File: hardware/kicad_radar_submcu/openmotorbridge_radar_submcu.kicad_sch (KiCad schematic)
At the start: 15 parts, among them J1 12V_RADAR_PWR, J2 JST_SH_4P_MR20, J3 PROG_UART_4P, J4 Taoglas_FXUWB10, SW1 BOOT_SW, SW2 RESET_SW, U1 ESP32-C5-WROOM-1U, U2 TPS7A0533, U3 DW3110

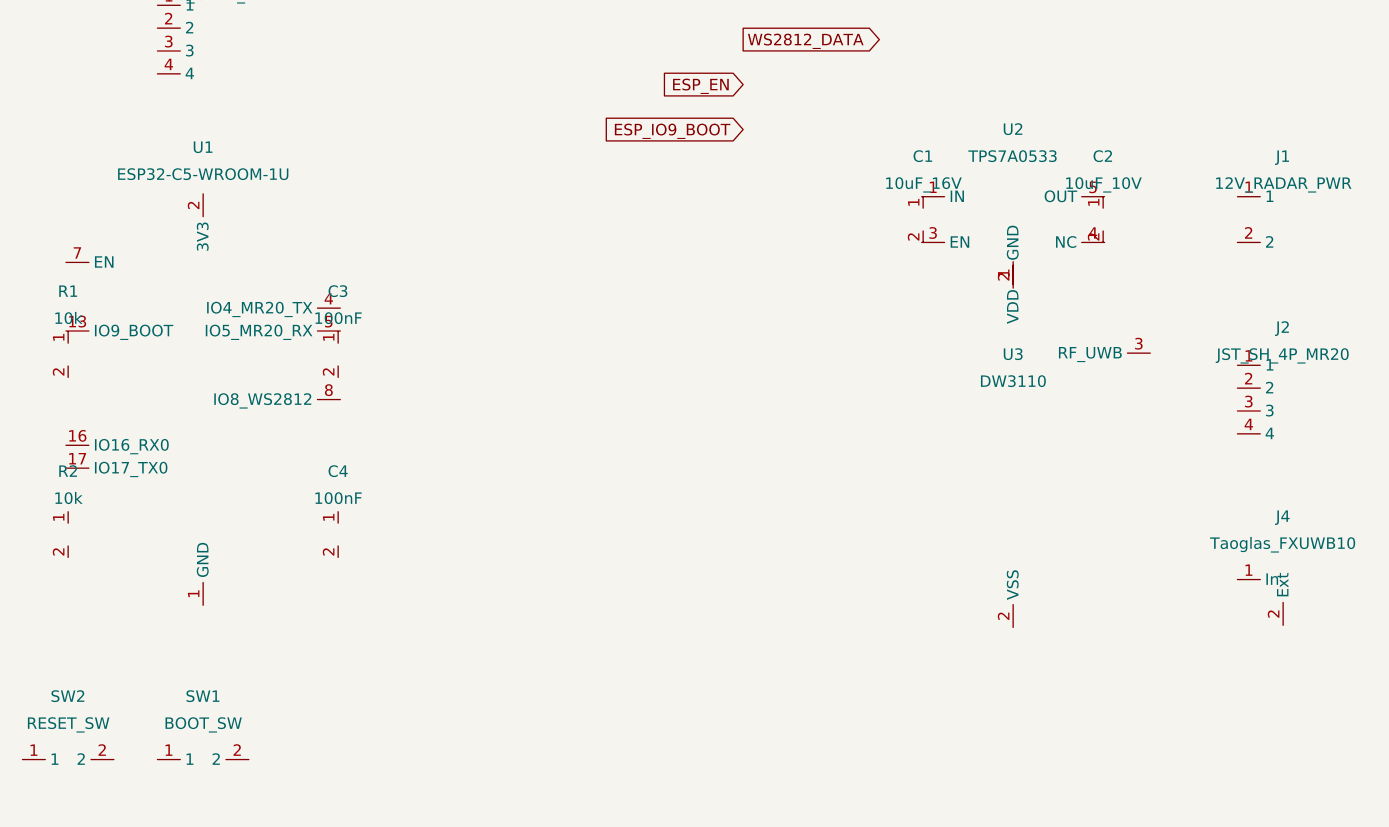
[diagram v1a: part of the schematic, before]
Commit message: feat(hw): finalize PCB lineup routing, sync PCBA 03 cartridge with J_PROG header and DTM12 schematics
- PCBA 01 (Central Box): Remediate net routing, DTM12 hierarchical schematic synchronization, 100% routed, 0 DRC errors.
- PCBA 03 (Smart Modular Cartridge): Position and route J_PROG 4-pin SMD programming header on F.Cu at (108.0, 89.61), synchronize CPL and schematic, 100% routed, 0 DRC errors.
- PCBA 05 (Universal Front Node): Preconnect and routing verified, 100% routed, 0 DRC errors.
- PCBA 07 (LoRa Smart-Keyfob): Routing and DRC verified, 100% routed, 0 DRC errors.
- PCBA 08 (Radar 2.0 Sub-MCU & Wings): Sub-MCU routing and HF isolation verified, 100% routed, 0 DRC errors.
- PCBA 10 (OMM 446 PMR/DMR Intercom): KiCad DRC verified, 100% routed, 0 DRC errors.
- Firmware: Align configuration headers across front_node and smart_cartridge.
- Tools: Add comprehensive preflight PCBA audit suite tools/audit_pcbas_preflight.py.
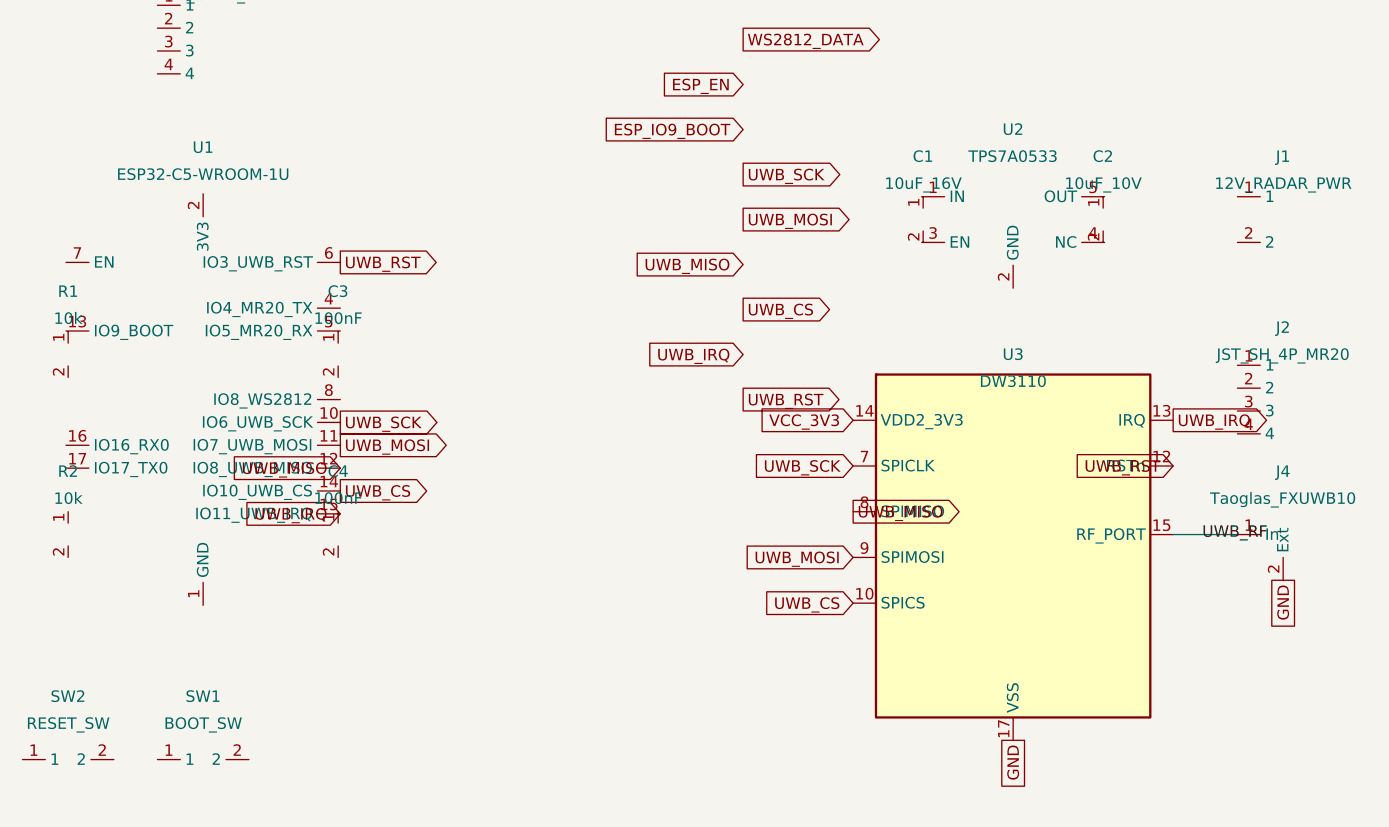
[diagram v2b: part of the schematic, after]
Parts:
- U3: footprint RF_Module:DW3110 -> Package_DFN_QFN:QFN-16-1EP_3x3mm_P0.5mm_EP1.7x1.7mm_ThermalVias
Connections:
- net GND: now also J4.2 (Ext), U3.17 (VSS)
- net VCC_3V3: now also U3.14 (VDD2_3V3)
- net UWB_RF: now reaches J4.1 (In)
- net UWB_RF: now also U3.15 (RF_PORT)
- new net UWB_CS: U1.14 (IO10_UWB_CS), U3.10 (SPICS)
- new net UWB_IRQ: U1.15 (IO11_UWB_IRQ), U3.13 (IRQ)
- new net UWB_MISO: U1.12 (IO8_UWB_MISO), U3.8 (SPIMISO)
- new net UWB_MOSI: U1.11 (IO7_UWB_MOSI), U3.9 (SPIMOSI)
- new net UWB_RST: U1.6 (IO3_UWB_RST), U3.12 (RSTn)
- new net UWB_SCK: U1.10 (IO6_UWB_SCK), U3.7 (SPICLK)
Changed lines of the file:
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@@
 	(global_label "ESP_EN" (shape input) (at 120.0 65.0 180) (effects (font (size 1.27 1.27)) (justify right)))
 	(global_label "ESP_IO9_BOOT" (shape input) (at 120.0 70.0 180) (effects (font (size 1.27 1.27)) (justify right)))
+	(global_label "UWB_SCK" (shape output) (at 120.0 75.0 0) (effects (font (size 1.27 1.27)) (justify left)))
+	(global_label "UWB_MOSI" (shape output) (at 120.0 80.0 0) (effects (font (size 1.27 1.27)) (justify left)))
+	(global_label "UWB_MISO" (shape input) (at 120.0 85.0 180) (effects (font (size 1.27 1.27)) (justify right)))
+	(global_label "UWB_CS" (shape output) (at 120.0 90.0 0) (effects (font (size 1.27 1.27)) (justify left)))
+	(global_label "UWB_IRQ" (shape input) (at 120.0 95.0 180) (effects (font (size 1.27 1.27)) (justify right)))
+	(global_label "UWB_RST" (shape output) (at 120.0 100.0 0) (effects (font (size 1.27 1.27)) (justify left)))
 	(symbol (lib_id "RF_Module:ESP32-C5-WROOM-1U") (at 60.0 100.0 0) (unit 1)
 		(in_bom yes) (on_board yes) (dnp no)
@@
 		(pin "16")
 		(pin "17")
+		(pin "6")
+		(pin "10")
+		(pin "11")
+		(pin "12")
+		(pin "14")
+		(pin "15")
 	)
 	(symbol (lib_id "Regulator_Linear:TPS7A0533") (at 150.0 80.0 0) (unit 1)
@@
 		(pin "5")
 	)
-	(symbol (lib_id "RF_Module:DW3110") (at 150.0 105.0 0) (unit 1)
+	(symbol (lib_id "RF_Module:DW3110") (at 150.0 115.0 0) (unit 1)
 		(in_bom yes) (on_board yes) (dnp no)
 		(property "Reference" "U3" (at 150.0 95.0 0) (effects (font (size 1.27 1.27))))
 		(property "Value" "DW3110" (at 150.0 98.0 0) (effects (font (size 1.27 1.27))))
-		(property "Footprint" "RF_Module:DW3110" (at 0 0 0) (effects (font (size 1.27 1.27)) hide))
+		(property "Footprint" "Package_DFN_QFN:QFN-16-1EP_3x3mm_P0.5mm_EP1.7x1.7mm_ThermalVias" (at 0 0 0) (effects (font (size 1.27 1.27)) hide))
+		(pin "14")
+		(pin "7")
+		(pin "8")
+		(pin "9")
+		(pin "10")
+		(pin "13")
+		(pin "12")
+		(pin "15")
+		(pin "17")
+	)
+	(symbol (lib_id "Connector:Conn_Coaxial") (at 180.0 115.0 0) (unit 1)
+		(in_bom yes) (on_board yes) (dnp no)
+		(property "Reference" "J4" (at 180.0 108.0 0) (effects (font (size 1.27 1.27))))
+		(property "Value" "Taoglas_FXUWB10" (at 180.0 111.0 0) (effects (font (size 1.27 1.27))))
+		(property "Footprint" "Connector_Coaxial:U.FL_Hirose_U.FL-R-SMT-1_Vertical" (at 0 0 0) (effects (font (size 1.27 1.27)) hide))
 		(pin "1")
 		(pin "2")
-		(pin "3")
 	)
 	(symbol (lib_id "Connector:Conn_01x02") (at 180.0 80.0 0) (unit 1)
@@
 		(pin "3")
 		(pin "4")
-	)
-	(symbol (lib_id "Connector:Conn_Coaxial") (at 180.0 120.0 0) (unit 1)
-		(in_bom yes) (on_board yes) (dnp no)
-		(property "Reference" "J4" (at 180.0 113.0 0) (effects (font (size 1.27 1.27))))
-		(property "Value" "Taoglas_FXUWB10" (at 180.0 116.0 0) (effects (font (size 1.27 1.27))))
-		(property "Footprint" "Connector_Coaxial:U.FL_Hirose_U.FL-R-SMT-1_Vertical" (at 0 0 0) (effects (font (size 1.27 1.27)) hide))
-		(pin "1")
-		(pin "2")
 	)
 	(symbol (lib_id "Switch:SW_Push") (at 60.0 140.0 0) (unit 1)
@@
 		(pin "2")
 	)
+	(global_label "UWB_RST" (shape output) (at 75.24 84.76 0) (effects (font (size 1.27 1.27)) (justify left)))
+	(global_label "UWB_SCK" (shape output) (at 75.24 102.54 0) (effects (font (size 1.27 1.27)) (justify left)))
+	(global_label "UWB_MOSI" (shape output) (at 75.24 105.08 0) (effects (font (size 1.27 1.27)) (justify left)))
+	(global_label "UWB_MISO" (shape input) (at 75.24 107.62 180) (effects (font (size 1.27 1.27)) (justify right)))
+	(global_label "UWB_CS" (shape output) (at 75.24 110.16 0) (effects (font (size 1.27 1.27)) (justify left)))
+	(global_label "UWB_IRQ" (shape input) (at 75.24 112.70 180) (effects (font (size 1.27 1.27)) (justify right)))
+	(global_label "VCC_3V3" (shape input) (at 132.22 102.30 180) (effects (font (size 1.27 1.27)) (justify right)))
+	(global_label "UWB_SCK" (shape input) (at 132.22 107.38 180) (effects (font (size 1.27 1.27)) (justify right)))
+	(global_label "UWB_MISO" (shape output) (at 132.22 112.46 0) (effects (font (size 1.27 1.27)) (justify left)))
+	(global_label "UWB_MOSI" (shape input) (at 132.22 117.54 180) (effects (font (size 1.27 1.27)) (justify right)))
+	(global_label "UWB_CS" (shape input) (at 132.22 122.62 180) (effects (font (size 1.27 1.27)) (justify right)))
+	(global_label "UWB_IRQ" (shape output) (at 167.78 102.30 0) (effects (font (size 1.27 1.27)) (justify left)))
+	(global_label "UWB_RST" (shape input) (at 167.78 107.38 180) (effects (font (size 1.27 1.27)) (justify right)))
+	(global_label "GND" (shape passive) (at 150.00 137.86 270) (effects (font (size 1.27 1.27)) (justify right)))
+	(wire (pts (xy 167.78 115.00) (xy 174.92 115.00)) (stroke (width 0) (type default)))
+	(label "UWB_RF" (at 171.00 115.00 0) (effects (font (size 1.27 1.27))))
+	(global_label "GND" (shape passive) (at 180.00 120.08 270) (effects (font (size 1.27 1.27)) (justify right)))
 )

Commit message: fix(radar-submcu): synchronize PCBA 08 schematic with PCB and pass prefab-gate check
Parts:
- removed C1: 10uF_16V, Capacitor_SMD:C_0805_2012Metric, symbol Device:C_Small
- removed C2: 10uF_10V, Capacitor_SMD:C_0805_2012Metric, symbol Device:C_Small
- removed C3, C4: 100nF, Capacitor_SMD:C_0603_1608Metric, symbol Device:C_Small
- removed J1: 12V_RADAR_PWR, Connector_JST:JST_JWPF_B02B-JWPF-SK-R_1x02_P2.00mm_Vertical, symbol Connector:Conn_01x02
- removed J2: JST_SH_4P_MR20, Connector_JST:JST_SH_SM04B-SRSS-TB_1x04-1MP_P1.00mm_Horizontal, symbol Connector:Conn_01x04
- removed J3: PROG_UART_4P, Connector_PinHeader_2.54mm:PinHeader_1x04_P2.54mm_Horizontal, symbol Connector:Conn_01x04
- removed J4: Taoglas_FXUWB10, Connector_Coaxial:U.FL_Hirose_U.FL-R-SMT-1_Vertical, symbol Connector:Conn_Coaxial
- removed R1, R2: 10k, Resistor_SMD:R_0603_1608Metric, symbol Device:R_Small
- removed SW1: BOOT_SW, Button_Switch_SMD:SW_Push_SPST_NO_Alps_SKRK, symbol Switch:SW_Push
- removed SW2: RESET_SW, Button_Switch_SMD:SW_Push_SPST_NO_Alps_SKRK, symbol Switch:SW_Push
- removed U1: ESP32-C5-WROOM-1U, RF_Module:ESP32-C3-WROOM-02U, symbol RF_Module:ESP32-C5-WROOM-1U
- removed U2: TPS7A0533, Package_TO_SOT_SMD:SOT-23-5, symbol Regulator_Linear:TPS7A0533
- removed U3: DW3110, Package_DFN_QFN:QFN-16-1EP_3x3mm_P0.5mm_EP1.7x1.7mm_ThermalVias, symbol RF_Module:DW3110
- added C1: 10uF_16V, C_0805_2012Metric, symbol C1_sym
- added C2: 10uF_10V, C_0805_2012Metric, symbol C2_sym
- added C3: 100nF, C_0603_1608Metric, symbol C3_sym
- added C4: 100nF, C_0603_1608Metric, symbol C4_sym
- added D1: WS2812B-2020, LED_WS2812B-2020_PLCC4_2.0x2.0mm, symbol D1_sym
- added D10: WS2812B-2020, LED_WS2812B-2020_PLCC4_2.0x2.0mm, symbol D10_sym
- added D11: WS2812B-2020, LED_WS2812B-2020_PLCC4_2.0x2.0mm, symbol D11_sym
- added D12: WS2812B-2020, LED_WS2812B-2020_PLCC4_2.0x2.0mm, symbol D12_sym
- added D13: WS2812B-2020, LED_WS2812B-2020_PLCC4_2.0x2.0mm, symbol D13_sym
- added D14: WS2812B-2020, LED_WS2812B-2020_PLCC4_2.0x2.0mm, symbol D14_sym
- added D15: WS2812B-2020, LED_WS2812B-2020_PLCC4_2.0x2.0mm, symbol D15_sym
- added D16: WS2812B-2020, LED_WS2812B-2020_PLCC4_2.0x2.0mm, symbol D16_sym
- added D17: WS2812B-2020, LED_WS2812B-2020_PLCC4_2.0x2.0mm, symbol D17_sym
- added D18: WS2812B-2020, LED_WS2812B-2020_PLCC4_2.0x2.0mm, symbol D18_sym
- added D19: WS2812B-2020, LED_WS2812B-2020_PLCC4_2.0x2.0mm, symbol D19_sym
- added D2: WS2812B-2020, LED_WS2812B-2020_PLCC4_2.0x2.0mm, symbol D2_sym
- added D20: WS2812B-2020, LED_WS2812B-2020_PLCC4_2.0x2.0mm, symbol D20_sym
- added D21: WS2812B-2020, LED_WS2812B-2020_PLCC4_2.0x2.0mm, symbol D21_sym
- added D22: WS2812B-2020, LED_WS2812B-2020_PLCC4_2.0x2.0mm, symbol D22_sym
- added D23: WS2812B-2020, LED_WS2812B-2020_PLCC4_2.0x2.0mm, symbol D23_sym
- added D24: WS2812B-2020, LED_WS2812B-2020_PLCC4_2.0x2.0mm, symbol D24_sym
- added D25: WS2812B-2020, LED_WS2812B-2020_PLCC4_2.0x2.0mm, symbol D25_sym
- added D26: WS2812B-2020, LED_WS2812B-2020_PLCC4_2.0x2.0mm, symbol D26_sym
- added D27: WS2812B-2020, LED_WS2812B-2020_PLCC4_2.0x2.0mm, symbol D27_sym
- added D28: WS2812B-2020, LED_WS2812B-2020_PLCC4_2.0x2.0mm, symbol D28_sym
- added D29: WS2812B-2020, LED_WS2812B-2020_PLCC4_2.0x2.0mm, symbol D29_sym
- added D3: WS2812B-2020, LED_WS2812B-2020_PLCC4_2.0x2.0mm, symbol D3_sym
- added D30: WS2812B-2020, LED_WS2812B-2020_PLCC4_2.0x2.0mm, symbol D30_sym
- added D31: WS2812B-2020, LED_WS2812B-2020_PLCC4_2.0x2.0mm, symbol D31_sym
- added D32: WS2812B-2020, LED_WS2812B-2020_PLCC4_2.0x2.0mm, symbol D32_sym
- added D33: WS2812B-2020, LED_WS2812B-2020_PLCC4_2.0x2.0mm, symbol D33_sym
- added D34: WS2812B-2020, LED_WS2812B-2020_PLCC4_2.0x2.0mm, symbol D34_sym
- added D35: WS2812B-2020, LED_WS2812B-2020_PLCC4_2.0x2.0mm, symbol D35_sym
- added D36: WS2812B-2020, LED_WS2812B-2020_PLCC4_2.0x2.0mm, symbol D36_sym
- added D4: WS2812B-2020, LED_WS2812B-2020_PLCC4_2.0x2.0mm, symbol D4_sym
- added D5: WS2812B-2020, LED_WS2812B-2020_PLCC4_2.0x2.0mm, symbol D5_sym
- added D6: WS2812B-2020, LED_WS2812B-2020_PLCC4_2.0x2.0mm, symbol D6_sym
- added D7: WS2812B-2020, LED_WS2812B-2020_PLCC4_2.0x2.0mm, symbol D7_sym
- added D8: WS2812B-2020, LED_WS2812B-2020_PLCC4_2.0x2.0mm, symbol D8_sym
- added D9: WS2812B-2020, LED_WS2812B-2020_PLCC4_2.0x2.0mm, symbol D9_sym
- added H1: M2.5_MountingHole, MountingHole_2.7mm_M2.5_Pad, symbol H1_sym
- added H2: M2.5_MountingHole, MountingHole_2.7mm_M2.5_Pad, symbol H2_sym
- added H3: M2.5_MountingHole, MountingHole_2.7mm_M2.5_Pad, symbol H3_sym
- added H4: M2.5_MountingHole, MountingHole_2.7mm_M2.5_Pad, symbol H4_sym
- added J1: 12V_RADAR_PWR, Connector_JST:JST_JWPF_B02B-JWPF-SK-R_1x02_P2.00mm_Vertical, symbol J1_sym
- added J2: JST_SH_4P_MR20, JST_SH_SM04B-SRSS-TB_1x04-1MP_P1.00mm_Horizontal, symbol J2_sym
- added J3: PROG_UART_4P, PinHeader_1x04_P2.54mm_Horizontal, symbol J3_sym
- added J4: Taoglas_FXUWB10, Connector_Coaxial:U.FL_Hirose_U.FL-R-SMT-1_Vertical, symbol J4_sym
- added R1: 10k, R_0603_1608Metric, symbol R1_sym
- added R2: 10k, R_0603_1608Metric, symbol R2_sym
- added SW1: BOOT_SW, SW_Push_SPST_NO_Alps_SKRK, symbol SW1_sym
- added SW2: RESET_SW, SW_Push_SPST_NO_Alps_SKRK, symbol SW2_sym
- added U1: ESP32-C5-WROOM-1U, ESP32-C3-WROOM-02U, symbol U1_sym
- added U2: TPS7A0533, SOT-23-5, symbol U2_sym
- added U3: DW3110, Package_DFN_QFN:QFN-16-1EP_3x3mm_P0.5mm_EP1.7x1.7mm_ThermalVias, symbol U3_sym
- added Y1_UWB: 38.4MHz, Crystal:Crystal_SMD_2016-4Pin_2.0x1.6mm, symbol Y1_UWB_sym
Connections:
- net CENTRAL_RX: now also J3.3 (CENTRAL_RX), U1.17 (CENTRAL_RX)
- net CENTRAL_TX: now also J3.2 (CENTRAL_TX), U1.16 (CENTRAL_TX)
- net ESP_EN: now also R1.2 (ESP_EN), SW2.1 (ESP_EN), U1.7 (ESP_EN)
- net ESP_IO9_BOOT: now also R2.2 (ESP_IO9_BOOT), SW1.1 (ESP_IO9_BOOT), U1.13 (ESP_IO9_BOOT)
- net GND: now also C1.2 (GND), C2.2 (GND), C3.2 (GND), C4.2 (GND), D1.3 (GND), D10.3 (GND), D11.3 (GND), D12.3 (GND), D13.3 (GND), D14.3 (GND), D15.3 (GND), D16.3 (GND), D17.3 (GND), D18.3 (GND), D19.3 (GND), D2.3 (GND), D20.3 (GND), D21.3 (GND), D22.3 (GND), D23.3 (GND), D24.3 (GND), D25.3 (GND), D26.3 (GND), D27.3 (GND), D28.3 (GND), D29.3 (GND), D3.3 (GND), D30.3 (GND), D31.3 (GND), D32.3 (GND), D33.3 (GND), D34.3 (GND), D35.3 (GND), D36.3 (GND), D4.3 (GND), D5.3 (GND), D6.3 (GND), D7.3 (GND), D8.3 (GND), D9.3 (GND), H1.1 (GND), H2.1 (GND), H3.1 (GND), H4.1 (GND), J1.2 (GND), J2.2 (GND), J2.MP (GND), J3.4 (GND), J4.2 (GND), SW1.2 (GND), SW2.2 (GND), U1.1 (GND), U1.18 (GND), U1.19 (GND), U1.9 (GND), U2.2 (GND), U3.16 (GND), U3.17 (GND), Y1_UWB.2 (GND), Y1_UWB.4 (GND)
- net MR20_RX: now also J2.4 (MR20_RX), U1.5 (MR20_RX)
- net MR20_TX: now also J2.3 (MR20_TX), U1.4 (MR20_TX)
- net UWB_CS: now also U1.14 (UWB_CS), U3.10 (UWB_CS)
- net UWB_IRQ: now also U1.15 (UWB_IRQ), U3.13 (UWB_IRQ)
- net UWB_MISO: now also U1.12 (UWB_MISO), U3.8 (UWB_MISO)
- net UWB_MOSI: now also U1.11 (UWB_MOSI), U3.9 (UWB_MOSI)
- net UWB_RF: now also J4.1 (UWB_RF), U3.15 (UWB_RF)
- net UWB_RST: now also U1.6 (UWB_RST), U3.12 (UWB_RST)
- net UWB_SCK: now also U1.10 (UWB_SCK), U3.7 (UWB_SCK)
- net VCC_3V3: now also C2.1 (VCC_3V3), C3.1 (VCC_3V3), C4.1 (VCC_3V3), J3.1 (VCC_3V3), R1.1 (VCC_3V3), R2.1 (VCC_3V3), U1.2 (VCC_3V3), U2.5 (VCC_3V3), U3.14 (VCC_3V3)
- net VCC_5V: now also C1.1 (VCC_5V), D1.2 (VCC_5V), D10.2 (VCC_5V), D11.2 (VCC_5V), D12.2 (VCC_5V), D13.2 (VCC_5V), D14.2 (VCC_5V), D15.2 (VCC_5V), D16.2 (VCC_5V), D17.2 (VCC_5V), D18.2 (VCC_5V), D19.2 (VCC_5V), D2.2 (VCC_5V), D20.2 (VCC_5V), D21.2 (VCC_5V), D22.2 (VCC_5V), D23.2 (VCC_5V), D24.2 (VCC_5V), D25.2 (VCC_5V), D26.2 (VCC_5V), D27.2 (VCC_5V), D28.2 (VCC_5V), D29.2 (VCC_5V), D3.2 (VCC_5V), D30.2 (VCC_5V), D31.2 (VCC_5V), D32.2 (VCC_5V), D33.2 (VCC_5V), D34.2 (VCC_5V), D35.2 (VCC_5V), D36.2 (VCC_5V), D4.2 (VCC_5V), D5.2 (VCC_5V), D6.2 (VCC_5V), D7.2 (VCC_5V), D8.2 (VCC_5V), D9.2 (VCC_5V), J1.1 (VCC_5V), J2.1 (VCC_5V), U2.1 (VCC_5V), U2.3 (VCC_5V)
- net WS2812_DATA: now also D1.1 (WS2812_DATA), D1.4 (WS2812_DATA), D10.1 (WS2812_DATA), D10.4 (WS2812_DATA), D11.1 (WS2812_DATA), D11.4 (WS2812_DATA), D12.1 (WS2812_DATA), D12.4 (WS2812_DATA), D13.1 (WS2812_DATA), D13.4 (WS2812_DATA), D14.1 (WS2812_DATA), D14.4 (WS2812_DATA), D15.1 (WS2812_DATA), D15.4 (WS2812_DATA), D16.1 (WS2812_DATA), D16.4 (WS2812_DATA), D17.1 (WS2812_DATA), D17.4 (WS2812_DATA), D18.1 (WS2812_DATA), D18.4 (WS2812_DATA), D19.1 (WS2812_DATA), D19.4 (WS2812_DATA), D2.1 (WS2812_DATA), D2.4 (WS2812_DATA), D20.1 (WS2812_DATA), D20.4 (WS2812_DATA), D21.1 (WS2812_DATA), D21.4 (WS2812_DATA), D22.1 (WS2812_DATA), D22.4 (WS2812_DATA), D23.1 (WS2812_DATA), D23.4 (WS2812_DATA), D24.1 (WS2812_DATA), D24.4 (WS2812_DATA), D25.1 (WS2812_DATA), D25.4 (WS2812_DATA), D26.1 (WS2812_DATA), D26.4 (WS2812_DATA), D27.1 (WS2812_DATA), D27.4 (WS2812_DATA), D28.1 (WS2812_DATA), D28.4 (WS2812_DATA), D29.1 (WS2812_DATA), D29.4 (WS2812_DATA), D3.1 (WS2812_DATA), D3.4 (WS2812_DATA), D30.1 (WS2812_DATA), D30.4 (WS2812_DATA), D31.1 (WS2812_DATA), D31.4 (WS2812_DATA), D32.1 (WS2812_DATA), D32.4 (WS2812_DATA), D33.1 (WS2812_DATA), D33.4 (WS2812_DATA), D34.1 (WS2812_DATA), D34.4 (WS2812_DATA), D35.1 (WS2812_DATA), D35.4 (WS2812_DATA), D36.1 (WS2812_DATA), D36.4 (WS2812_DATA), D4.1 (WS2812_DATA), D4.4 (WS2812_DATA), D5.1 (WS2812_DATA), D5.4 (WS2812_DATA), D6.1 (WS2812_DATA), D6.4 (WS2812_DATA), D7.1 (WS2812_DATA), D7.4 (WS2812_DATA), D8.1 (WS2812_DATA), D8.4 (WS2812_DATA), D9.1 (WS2812_DATA), D9.4 (WS2812_DATA), U1.8 (WS2812_DATA)
- new net UWB_XTAL1: U3.4 (UWB_XTAL1), Y1_UWB.1 (UWB_XTAL1)
- new net UWB_XTAL2: U3.5 (UWB_XTAL2), Y1_UWB.3 (UWB_XTAL2)
